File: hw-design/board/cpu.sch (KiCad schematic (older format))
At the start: 22 parts, among them P1 CHAIN, P2 USB_OTG, P3 SWD, Q7 BC857, SW1 SW_PUSH, U4 LPC11U24FBD48/401, Y1 12MHz

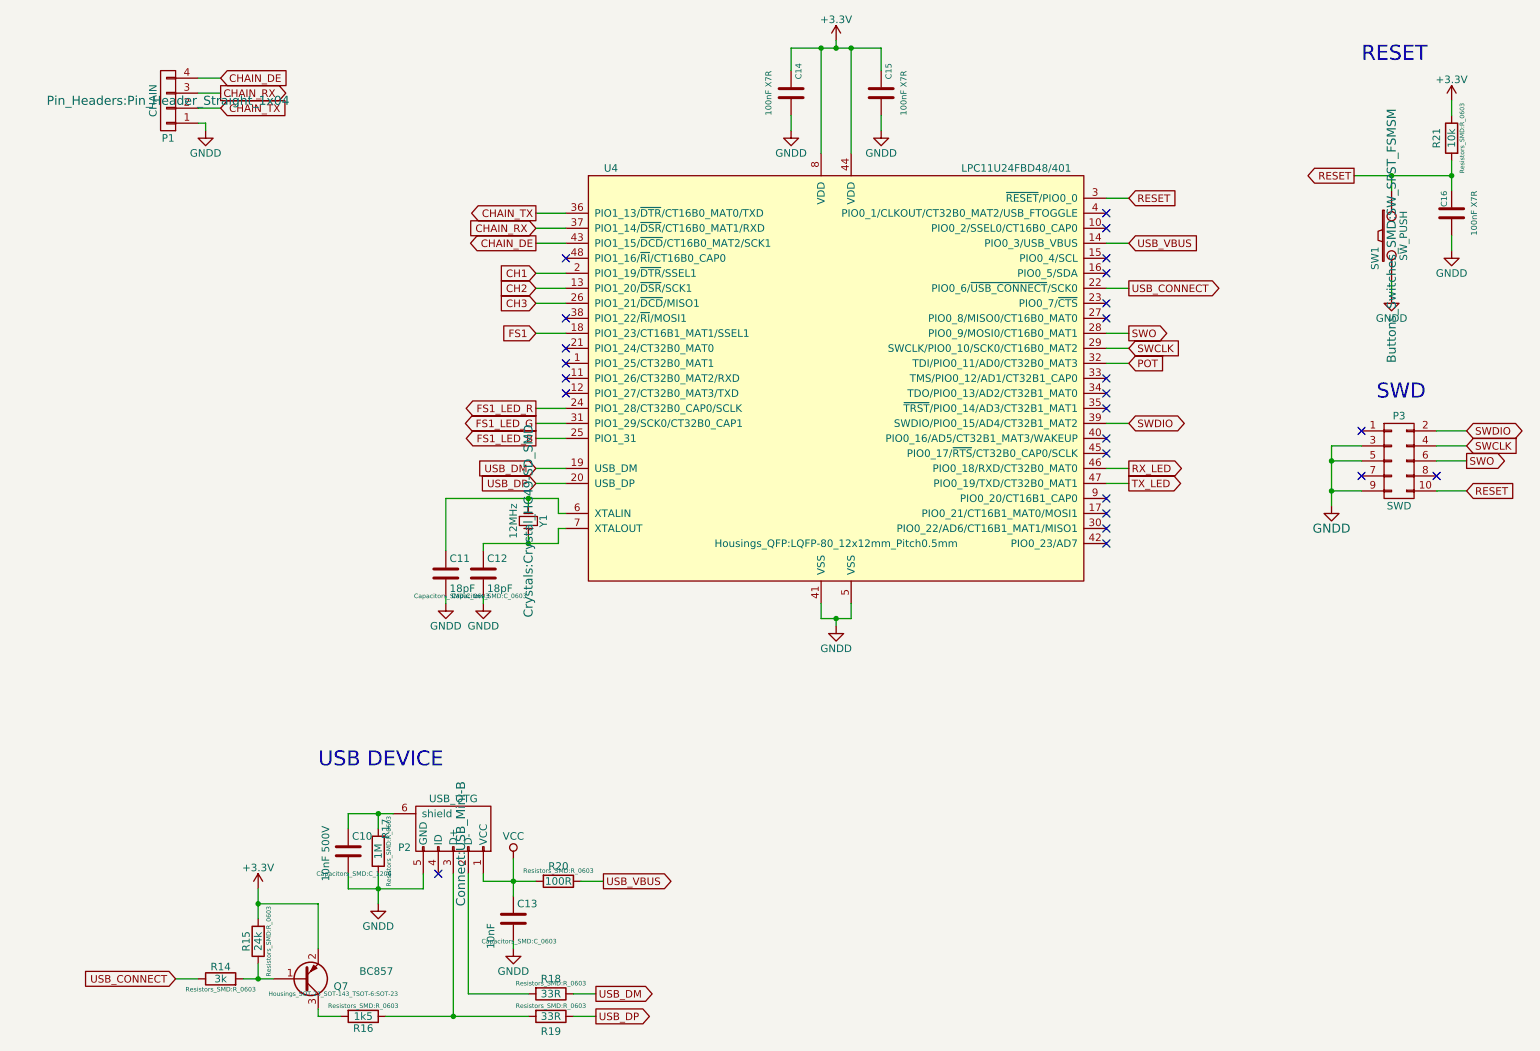
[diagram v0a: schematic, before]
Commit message: sch: fixing VBUS signal and FS1 I/O
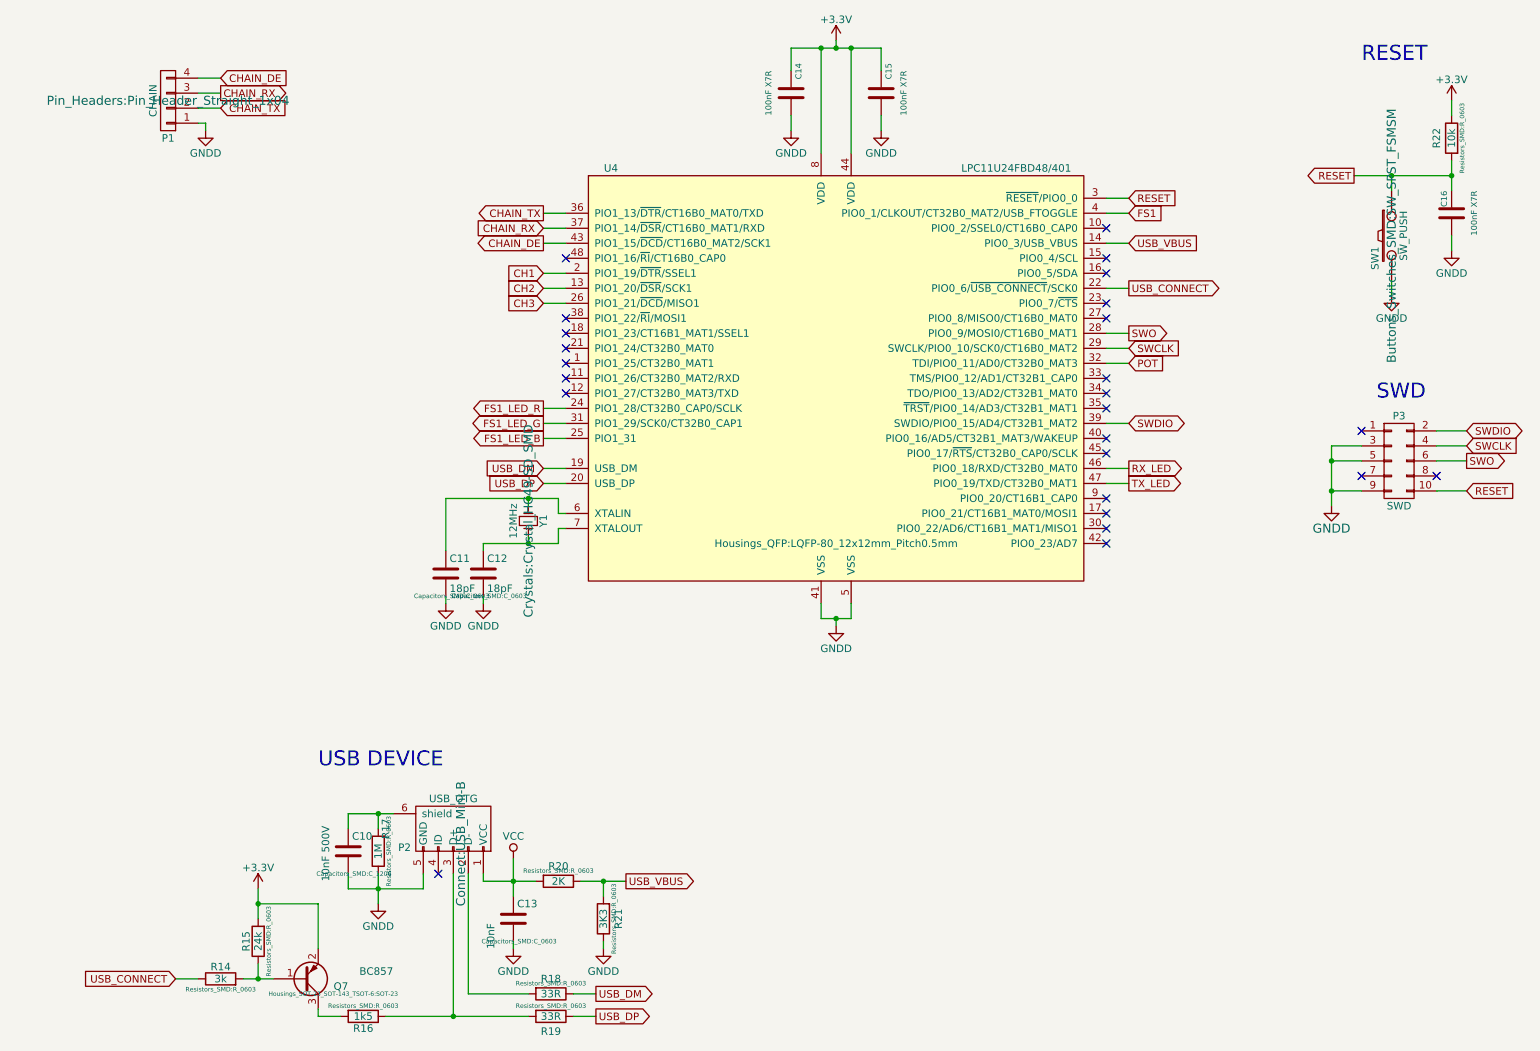
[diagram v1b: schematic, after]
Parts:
- added R21: 3K3, Resistors_SMD:R_0603, symbol R
- R20: value 100R -> 2K; MPN RMCF0603JT100R -> RMCF0603JT2K00
- renumbered R21 to R22
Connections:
- net FS1: now also U4.4 (PIO0_1/CLKOUT/CT32B0_MAT2/USB_FTOGGLE); no longer U4.18 (PIO1_23/CT16B1_MAT1/SSEL1)
- net GNDD: now also R21.1
- net USB_VBUS: now also R21.2
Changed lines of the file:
@@
 P 4050 6450
 F 0 "R20" V 3950 6450 50  0000 C CNN
-F 1 "100R" V 4050 6450 50  0000 C CNN
+F 1 "2K" V 4050 6450 50  0000 C CNN
 F 2 "Resistors_SMD:R_0603" V 3980 6450 30  0000 C CNN
 F 3 "" H 4050 6450 30  0000 C CNN
-F 4 "RMCF0603JT100R" H 0   0   50  0001 C CNN "MPN"
+F 4 "RMCF0603JT2K00" H 0   0   50  0001 C CNN "MPN"
 	1    4050 6450
 	0    1    1    0
@@
 $EndComp
 $Comp
-L R R21
+L R R22
 U 1 1 558018EB
 P 10000 1500
-F 0 "R21" V 10100 1500 50  0000 C CNN
+F 0 "R22" V 10100 1500 50  0000 C CNN
 F 1 "10k" V 10000 1500 50  0000 C CNN
 F 2 "Resistors_SMD:R_0603" V 9930 1500 30  0000 C CNN
@@
 Text GLabel 7850 2500 2    50   Output ~ 0
 USB_CONNECT
-Text GLabel 4350 6450 2    50   Output ~ 0
+Text GLabel 4500 6450 2    50   Output ~ 0
 USB_VBUS
 Text GLabel 4300 7200 2    50   Output ~ 0
@@
 Text GLabel 4300 7350 2    50   Output ~ 0
 USB_DP
-Text GLabel 3900 3700 0    50   Input ~ 0
+Text GLabel 3950 3700 0    50   Input ~ 0
 USB_DM
-Text GLabel 3900 3800 0    50   Input ~ 0
+Text GLabel 3950 3800 0    50   Input ~ 0
 USB_DP
 Text Notes 2450 5700 0    100  ~ 0
@@
 Text GLabel 1500 7100 0    50   Input ~ 0
 USB_CONNECT
-Text GLabel 3900 2000 0    50   Output ~ 0
+Text GLabel 3950 2000 0    50   Output ~ 0
 CHAIN_TX
-Text GLabel 3900 2100 0    50   Input ~ 0
+Text GLabel 3950 2100 0    50   Input ~ 0
 CHAIN_RX
-Text GLabel 3900 2200 0    50   Output ~ 0
+Text GLabel 3950 2200 0    50   Output ~ 0
 CHAIN_DE
 Text GLabel 1800 1300 2    50   Input ~ 0
@@
 Text GLabel 7850 3000 2    50   Input ~ 0
 POT
-Text GLabel 3900 2800 0    50   Input ~ 0
+Text GLabel 7850 2000 2    50   Input ~ 0
 FS1
-Text GLabel 3900 2400 0    50   Input ~ 0
+Text GLabel 3950 2400 0    50   Input ~ 0
 CH1
-Text GLabel 3900 2500 0    50   Input ~ 0
+Text GLabel 3950 2500 0    50   Input ~ 0
 CH2
-Text GLabel 3900 2600 0    50   Input ~ 0
+Text GLabel 3950 2600 0    50   Input ~ 0
 CH3
 Text GLabel 7850 3700 2    50   Output ~ 0
@@
 Text GLabel 7850 3800 2    50   Output ~ 0
 TX_LED
-Text GLabel 3900 3300 0    50   Output ~ 0
+Text GLabel 3950 3300 0    50   Output ~ 0
 FS1_LED_R
-Text GLabel 3900 3400 0    50   Output ~ 0
+Text GLabel 3950 3400 0    50   Output ~ 0
 FS1_LED_G
-Text GLabel 3900 3500 0    50   Output ~ 0
+Text GLabel 3950 3500 0    50   Output ~ 0
 FS1_LED_B
 Wire Wire Line
@@
 	3450 7200 3450 6400
 Wire Wire Line
-	4200 6450 4350 6450
+	4200 6450 4500 6450
 Wire Wire Line
 	3550 6450 3900 6450
@@
 	2850 6400 2850 6600
 Wire Wire Line
-	3900 3700 4100 3700
-Wire Wire Line
-	4100 3800 3900 3800
+	3950 3700 4100 3700
+Wire Wire Line
+	4100 3800 3950 3800
 Wire Wire Line
 	1950 7100 2150 7100
@@
 	3750 6900 3750 6850
 Wire Wire Line
-	3900 2000 4100 2000
-Wire Wire Line
-	3900 2100 4100 2100
-Wire Wire Line
-	4100 2200 3900 2200
+	3950 2000 4100 2000
+Wire Wire Line
+	3950 2100 4100 2100
+Wire Wire Line
+	4100 2200 3950 2200
 Wire Wire Line
 	1650 1300 1800 1300
@@
 	7850 3000 7700 3000
 Wire Wire Line
-	3900 2400 4100 2400
-Wire Wire Line
-	4100 2500 3900 2500
-Wire Wire Line
-	3900 2600 4100 2600
-Wire Wire Line
-	4100 2800 3900 2800
+	3950 2400 4100 2400
+Wire Wire Line
+	4100 2500 3950 2500
+Wire Wire Line
+	3950 2600 4100 2600
+Wire Wire Line
+	7700 2000 7850 2000
 Wire Wire Line
 	7850 3700 7700 3700
@@
 	7850 3800 7700 3800
 Wire Wire Line
-	4100 3300 3900 3300
-Wire Wire Line
-	3900 3400 4100 3400
-Wire Wire Line
-	4100 3500 3900 3500
+	4100 3300 3950 3300
+Wire Wire Line
+	3950 3400 4100 3400
+Wire Wire Line
+	4100 3500 3950 3500
 Connection ~ 9200 3650
 Connection ~ 9200 3850
@@
 NoConn ~ 4100 3100
 NoConn ~ 4100 3200
-NoConn ~ 7700 2000
+NoConn ~ 4100 2800
 NoConn ~ 7700 2100
 NoConn ~ 7700 2300
@@
 NoConn ~ 7700 4200
 NoConn ~ 4100 2300
+$Comp
+L R R21
+U 1 1 558BCA3B
+P 4350 6700
+F 0 "R21" V 4250 6700 50  0000 C CNN
+F 1 "3K3" V 4350 6700 50  0000 C CNN
+F 2 "Resistors_SMD:R_0603" V 4280 6700 30  0000 C CNN
+F 3 "" H 4350 6700 30  0000 C CNN
+F 4 "RMCF0603JT3K30" H 300 250 50  0001 C CNN "MPN"
+	1    4350 6700
+	-1   0    0    1
+$EndComp
+Wire Wire Line
+	4350 6550 4350 6450
+Connection ~ 4350 6450
+$Comp
+L GNDD #PWR060
+U 1 1 558BD1E6
+P 4350 6900
+F 0 "#PWR060" H 4350 6650 50  0001 C CNN
+F 1 "GNDD" H 4350 6750 50  0000 C CNN
+F 2 "" H 4350 6900 60  0000 C CNN
+F 3 "" H 4350 6900 60  0000 C CNN
+	1    4350 6900
+	1    0    0    -1
+$EndComp
+Wire Wire Line
+	4350 6900 4350 6850
 $EndSCHEMATC
